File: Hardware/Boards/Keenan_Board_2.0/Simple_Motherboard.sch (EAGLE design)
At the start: 102 parts, among them U1 WIZ811MJ, U1_MUX 74HC4052D,653, U2_MUX 74HC4052D,653, U3_MUX 74HC4052D,653, U4_MUX 74HC4052D,653, U5_MUX 74HC4052D,653, U7_MUX 74HC4052D,653

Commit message: Top Stellaris Connector Routed
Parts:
- removed JP2, JP3: (no value), SparkFun-Connectors:M04POLAR
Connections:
- removed net N$23: JP2.2, U$2.PD3
- removed net N$24: JP2.3, U$2.PF0
- removed net N$25: JP3.1, U$2.PF1
- removed net N$26: JP3.2, U$2.PF2
- removed net N$27: JP3.3, U$2.PF3
- removed net N$30: JP3.4, U$2.PF4
- removed net N$7: JP2.1, U$2.PD2
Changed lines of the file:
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@@
 <part name="P+26" library="supply1" deviceset="+5V" device=""/>
 <part name="P+27" library="supply1" deviceset="+5V" device=""/>
-<part name="JP2" library="SparkFun-Connectors" deviceset="M04" device="POLAR"/>
-<part name="JP3" library="SparkFun-Connectors" deviceset="M04" device="POLAR"/>
 </parts>
 <sheets>
@@
 <instance part="S1" gate="1" x="-33.02" y="-35.56"/>
 <instance part="U$2" gate="G$1" x="0" y="0"/>
-<instance part="JP2" gate="G$1" x="88.9" y="5.08" rot="R180"/>
-<instance part="JP3" gate="G$1" x="88.9" y="-17.78" rot="R180"/>
 </instances>
 <busses>
@@
 </segment>
 </net>
-<net name="N$7" class="0">
-<segment>
-<pinref part="U$2" gate="G$1" pin="PD2"/>
-<wire x1="15.24" y1="5.08" x2="71.12" y2="5.08" width="0.1524" layer="91"/>
-<wire x1="71.12" y1="5.08" x2="71.12" y2="7.62" width="0.1524" layer="91"/>
-<pinref part="JP2" gate="G$1" pin="1"/>
-<wire x1="71.12" y1="7.62" x2="83.82" y2="7.62" width="0.1524" layer="91"/>
-</segment>
-</net>
-<net name="N$23" class="0">
-<segment>
-<pinref part="U$2" gate="G$1" pin="PD3"/>
-<wire x1="15.24" y1="2.54" x2="73.66" y2="2.54" width="0.1524" layer="91"/>
-<wire x1="73.66" y1="2.54" x2="73.66" y2="5.08" width="0.1524" layer="91"/>
-<pinref part="JP2" gate="G$1" pin="2"/>
-<wire x1="73.66" y1="5.08" x2="83.82" y2="5.08" width="0.1524" layer="91"/>
-</segment>
-</net>
-<net name="N$24" class="0">
-<segment>
-<pinref part="U$2" gate="G$1" pin="PF0"/>
-<wire x1="15.24" y1="-12.7" x2="76.2" y2="-12.7" width="0.1524" layer="91"/>
-<wire x1="76.2" y1="-12.7" x2="76.2" y2="2.54" width="0.1524" layer="91"/>
-<pinref part="JP2" gate="G$1" pin="3"/>
-<wire x1="76.2" y1="2.54" x2="83.82" y2="2.54" width="0.1524" layer="91"/>
-</segment>
-</net>
-<net name="N$25" class="0">
-<segment>
-<pinref part="U$2" gate="G$1" pin="PF1"/>
-<pinref part="JP3" gate="G$1" pin="1"/>
-<wire x1="15.24" y1="-15.24" x2="83.82" y2="-15.24" width="0.1524" layer="91"/>
-</segment>
-</net>
-<net name="N$26" class="0">
-<segment>
-<pinref part="JP3" gate="G$1" pin="2"/>
-<pinref part="U$2" gate="G$1" pin="PF2"/>
-<wire x1="83.82" y1="-17.78" x2="15.24" y2="-17.78" width="0.1524" layer="91"/>
-</segment>
-</net>
-<net name="N$27" class="0">
-<segment>
-<pinref part="JP3" gate="G$1" pin="3"/>
-<pinref part="U$2" gate="G$1" pin="PF3"/>
-<wire x1="83.82" y1="-20.32" x2="15.24" y2="-20.32" width="0.1524" layer="91"/>
-</segment>
-</net>
-<net name="N$30" class="0">
-<segment>
-<pinref part="JP3" gate="G$1" pin="4"/>
-<pinref part="U$2" gate="G$1" pin="PF4"/>
-<wire x1="83.82" y1="-22.86" x2="15.24" y2="-22.86" width="0.1524" layer="91"/>
-</segment>
-</net>

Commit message: Lots of stuff
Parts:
- added C27, C28: 0.1uF, SparkFun-Passives:CAP1206
- added C29, C30: 22pF, SparkFun-Passives:CAP1206
- added GPS: M09, SparkFun-Connectors:M09
- added J1: AVR_SPI_PRG_6PTH, SparkFun-Connectors:AVR_SPI_PRG_6PTH
- added R38: 10k, SparkFun-Resistors:RESISTOR1206
- added U2: ATMEGA328P_PDIP, SparkFun-DigitalIC:ATMEGA328P_PDIP
- added Y1: 16MHz, SparkFun-FreqCtrl:CRYSTALHC49US
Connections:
- removed net N$10 (its old number): R4.1, RS-485-2.A, U$4.1
- removed net N$11 (its old number): R4.2, RS-485-2.B, U$4.2
- removed net N$13 (its old number): R7.2, RS-485-3.Z, U$5.6
- removed net N$16 (its old number): R7.1, RS-485-3.Y, U$5.3
- removed net N$18 (its old number): R8.1, RS-485-4.A, U$6.1
- removed net N$19 (its old number): R8.2, RS-485-4.B, U$6.2
- new net 328_RX: U2.PD0(RXD)
- new net 328_TX: U2.PD1(TXD)
- new net ATCLK3: C30.1, U2.PB7(XTAL2/TOSC2), Y1.1
- new net ATCLK4: C29.1, U2.PB6(XTAL1/TOSC1), Y1.2
- new net AT_MISO: J1.1, U2.PB4(MISO)
- new net AT_MOSI: J1.4, U2.PB3(MOSI/OC2)
- new net AT_SCK: J1.3, U2.PB5(SCK)
- new net N$12: R8.1, RS-485-3.Y, U$5.3
- new net N$22: R3.1, RS-485-2.A, U$4.1
- new net N$23: U$2.PF0
- new net N$24: U$2.PF1
- new net N$25: U$2.PF2
- new net N$26: U$2.PF3
- new net N$27: U$2.PF4
- new net N$28: R3.2, RS-485-2.B, U$4.2
- new net N$34: R7.1, RS-485-4.A, U$6.1
- new net N$35: R7.2, RS-485-4.B, U$6.2
- new net N$7: U$2.PD3
- new net N$8: R8.2, RS-485-3.Z, U$5.6
- net +5V: now also C27.1, C28.1, J1.2, R38.2, U2.AREF, U2.AVCC, U2.VCC
- net 10_RX+: now also R27.2, RS_TRANS_8.A; no longer R32.2, RS_TRANS_10.A
- net 10_RX-: now also R27.1, RS_TRANS_8.B; no longer R32.1, RS_TRANS_10.B
- net 10_TX+: now also R29.1, RS_TRANS_8.Y; no longer R33.1, RS_TRANS_10.Y
- net 10_TX-: now also R29.2, RS_TRANS_8.Z; no longer R33.2, RS_TRANS_10.Z
- net 11_RX+: now also R31.2, RS_TRANS_10.A; no longer R34.2, RS_TRANS_11.A
- net 11_RX-: now also R31.1, RS_TRANS_10.B; no longer R34.1, RS_TRANS_11.B
- net 11_TX+: now also R33.1, RS_TRANS_10.Y; no longer R35.1, RS_TRANS_11.Y
- net 11_TX-: now also R33.2, RS_TRANS_10.Z; no longer R35.2, RS_TRANS_11.Z
- net 12_RX+: now also R35.2; no longer R36.2
- net 12_RX-: now also R35.1; no longer R36.1
- net 1_TX+: now also R16.1; no longer R15.1
- net 1_TX-: now also R16.2; no longer R15.2
- net 2_RX+: now also R18.2, RS_TRANS_3.A; no longer R16.2, RS_TRANS_2.A
- net 2_RX-: now also R18.1, RS_TRANS_3.B; no longer R16.1, RS_TRANS_2.B
- net 2_TX+: now also R20.1, RS_TRANS_3.Y; no longer R17.1, RS_TRANS_2.Y
- net 2_TX-: now also R20.2, RS_TRANS_3.Z; no longer R17.2, RS_TRANS_2.Z
- net 3_RX+: now also R22.2, RS_TRANS_5.A; no longer R18.2, RS_TRANS_3.A
- net 3_RX-: now also R22.1, RS_TRANS_5.B; no longer R18.1, RS_TRANS_3.B
- net 3_TX+: now also R24.1, RS_TRANS_5.Y; no longer R19.1, RS_TRANS_3.Y
- net 3_TX-: now also R24.2, RS_TRANS_5.Z; no longer R19.2, RS_TRANS_3.Z
- net 4_RX+: now also R26.2, RS_TRANS_7.A; no longer R20.2, RS_TRANS_4.A
- net 4_RX-: now also R26.1, RS_TRANS_7.B; no longer R20.1, RS_TRANS_4.B
- net 4_TX+: now also R28.1, RS_TRANS_7.Y; no longer R21.1, RS_TRANS_4.Y
- net 4_TX-: now also R28.2, RS_TRANS_7.Z; no longer R21.2, RS_TRANS_4.Z
- net 5_RX+: now also R30.2, RS_TRANS_9.A; no longer R22.2, RS_TRANS_5.A
- net 5_RX-: now also R30.1, RS_TRANS_9.B; no longer R22.1, RS_TRANS_5.B
- net 5_TX+: now also R32.1, RS_TRANS_9.Y; no longer R23.1, RS_TRANS_5.Y
- net 5_TX-: now also R32.2, RS_TRANS_9.Z; no longer R23.2, RS_TRANS_5.Z
- net 6_RX+: now also R34.2, RS_TRANS_11.A; no longer R24.2, RS_TRANS_6.A
- net 6_RX-: now also R34.1, RS_TRANS_11.B; no longer R24.1, RS_TRANS_6.B
- net 6_TX+: now also R36.1, RS_TRANS_11.Y; no longer R25.1, RS_TRANS_6.Y
- net 6_TX-: now also R36.2, RS_TRANS_11.Z; no longer R25.2, RS_TRANS_6.Z
- net 7_RX+: now also R15.2, RS_TRANS_2.A; no longer R26.2, RS_TRANS_7.A
- net 7_RX-: now also R15.1, RS_TRANS_2.B; no longer R26.1, RS_TRANS_7.B
- net 7_TX+: now also R17.1, RS_TRANS_2.Y; no longer R27.1, RS_TRANS_7.Y
- net 7_TX-: now also R17.2, RS_TRANS_2.Z; no longer R27.2, RS_TRANS_7.Z
- net 8_RX+: now also R19.2, RS_TRANS_4.A; no longer R28.2, RS_TRANS_8.A
- net 8_RX-: now also R19.1, RS_TRANS_4.B; no longer R28.1, RS_TRANS_8.B
- net 8_TX+: now also R21.1, RS_TRANS_4.Y; no longer R29.1, RS_TRANS_8.Y
- net 8_TX-: now also R21.2, RS_TRANS_4.Z; no longer R29.2, RS_TRANS_8.Z
- net 9_RX+: now also R23.2, RS_TRANS_6.A; no longer R30.2, RS_TRANS_9.A
- net 9_RX-: now also R23.1, RS_TRANS_6.B; no longer R30.1, RS_TRANS_9.B
- net 9_TX+: now also R25.1, RS_TRANS_6.Y; no longer R31.1, RS_TRANS_9.Y
- net 9_TX-: now also R25.2, RS_TRANS_6.Z; no longer R31.2, RS_TRANS_9.Z
- net GND: now also C27.2, C28.2, C29.2, C30.2, J1.6, U2.GND@1, U2.GND@2
- net N$4: now also R4.1; no longer R3.1
- net N$9: now also R4.2; no longer R3.2
- net RESET: now also J1.5, R38.1, U2.PC6(/RESET)
- net RS485_10_RX: now also RS_TRANS_8.R0; no longer RS_TRANS_10.R0
- net RS485_10_TX: now also RS_TRANS_8.DI; no longer RS_TRANS_10.DI
- net RS485_11_RX: now also RS_TRANS_10.R0; no longer RS_TRANS_11.R0
- net RS485_11_TX: now also RS_TRANS_10.DI; no longer RS_TRANS_11.DI
- net RS485_14_RX: now also RS-485-3.R0; no longer RS-485-2.R0
- net RS485_14_TX: now also RS-485-3.DI; no longer RS-485-2.DI
- net RS485_15_RX: now also RS-485-5.R0; no longer RS-485-3.R0
- net RS485_15_TX: now also RS-485-5.DI; no longer RS-485-3.DI
- net RS485_16_RX: now also RS-485-6.R0; no longer RS-485-4.R0
- net RS485_16_TX: now also RS-485-6.DI; no longer RS-485-4.DI
- net RS485_17_RX: now also RS-485-2.R0; no longer RS-485-5.R0
- net RS485_17_TX: now also RS-485-2.DI; no longer RS-485-5.DI
- net RS485_18_RX: now also RS-485-4.R0; no longer RS-485-6.R0
- net RS485_18_TX: now also RS-485-4.DI; no longer RS-485-6.DI
- net RS485_2_RX: now also RS_TRANS_3.R0; no longer RS_TRANS_2.R0
- net RS485_2_TX: now also RS_TRANS_3.DI; no longer RS_TRANS_2.DI
- net RS485_3_RX: now also RS_TRANS_5.R0; no longer RS_TRANS_3.R0
- net RS485_3_TX: now also RS_TRANS_5.DI; no longer RS_TRANS_3.DI
- net RS485_4_RX: now also RS_TRANS_7.R0; no longer RS_TRANS_4.R0
- net RS485_4_TX: now also RS_TRANS_7.DI; no longer RS_TRANS_4.DI
- net RS485_5_RX: now also RS_TRANS_9.R0; no longer RS_TRANS_5.R0
- net RS485_5_TX: now also RS_TRANS_9.DI; no longer RS_TRANS_5.DI
- net RS485_6_RX: now also RS_TRANS_11.R0; no longer RS_TRANS_6.R0
- net RS485_6_TX: now also RS_TRANS_11.DI; no longer RS_TRANS_6.DI
- net RS485_7_RX: now also RS_TRANS_2.R0; no longer RS_TRANS_7.R0
- net RS485_7_TX: now also RS_TRANS_2.DI; no longer RS_TRANS_7.DI
- net RS485_8_RX: now also RS_TRANS_4.R0; no longer RS_TRANS_8.R0
- net RS485_8_TX: now also RS_TRANS_4.DI; no longer RS_TRANS_8.DI
- net RS485_9_RX: now also RS_TRANS_6.R0; no longer RS_TRANS_9.R0
- net RS485_9_TX: now also RS_TRANS_6.DI; no longer RS_TRANS_9.DI

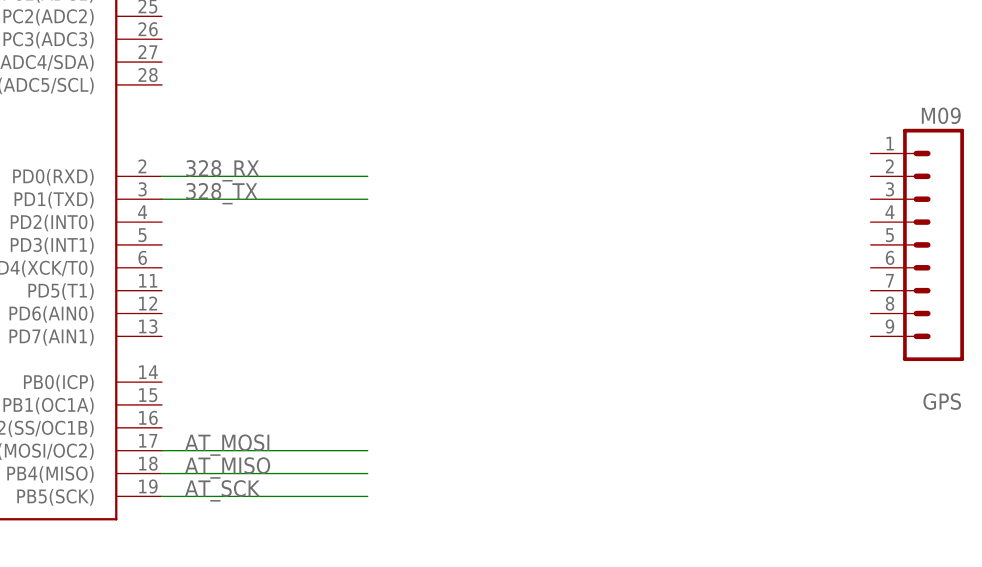
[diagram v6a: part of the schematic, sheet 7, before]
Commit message: Added GPS to schematic
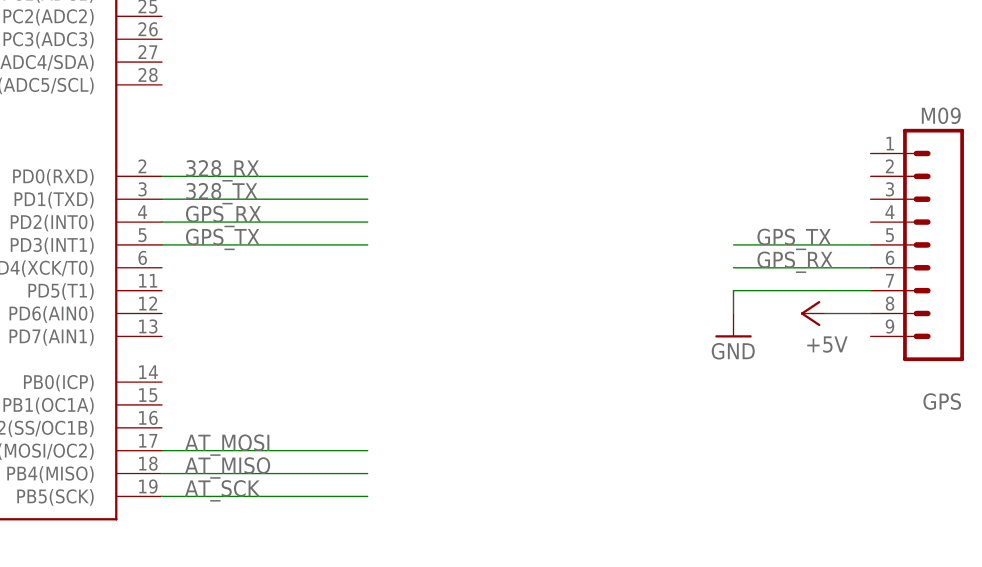
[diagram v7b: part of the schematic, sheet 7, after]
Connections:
- new net GPS_RX: GPS.6, U2.PD2(INT0)
- new net GPS_TX: GPS.5, U2.PD3(INT1)
- net +5V: now also GPS.8
- net GND: now also GPS.7
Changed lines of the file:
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@@
 <part name="GND35" library="supply1" deviceset="GND" device=""/>
 <part name="GPS" library="SparkFun-Connectors" deviceset="M09" device=""/>
+<part name="P+31" library="supply1" deviceset="+5V" device=""/>
+<part name="GND36" library="supply1" deviceset="GND" device=""/>
 </parts>
 <sheets>
@@
 <instance part="GND35" gate="1" x="25.4" y="-73.66"/>
 <instance part="GPS" gate="G$1" x="114.3" y="-5.08" rot="R180"/>
+<instance part="P+31" gate="1" x="96.52" y="-12.7" rot="R90"/>
+<instance part="GND36" gate="1" x="88.9" y="-15.24"/>
 </instances>
 <busses>
@@
 <wire x1="25.4" y1="-63.5" x2="25.4" y2="-71.12" width="0.1524" layer="91"/>
 </segment>
+<segment>
+<pinref part="GND36" gate="1" pin="GND"/>
+<wire x1="88.9" y1="-12.7" x2="88.9" y2="-10.16" width="0.1524" layer="91"/>
+<pinref part="GPS" gate="G$1" pin="7"/>
+<wire x1="88.9" y1="-10.16" x2="104.14" y2="-10.16" width="0.1524" layer="91"/>
+</segment>
 </net>
 <net name="ATCLK3" class="0">
@@
 <wire x1="25.4" y1="-58.42" x2="25.4" y2="-53.34" width="0.1524" layer="91"/>
 </segment>
+<segment>
+<pinref part="P+31" gate="1" pin="+5V"/>
+<pinref part="GPS" gate="G$1" pin="8"/>
+<wire x1="99.06" y1="-12.7" x2="104.14" y2="-12.7" width="0.1524" layer="91"/>
+</segment>
 </net>
 <net name="328_RX" class="0">
@@
 </segment>
 </net>
+<net name="GPS_RX" class="0">
+<segment>
+<pinref part="GPS" gate="G$1" pin="6"/>
+<wire x1="104.14" y1="-7.62" x2="88.9" y2="-7.62" width="0.1524" layer="91"/>
+<label x="91.44" y="-7.62" size="1.778" layer="95"/>
+</segment>
+<segment>
+<pinref part="U2" gate="G$1" pin="PD2(INT0)"/>
+<wire x1="25.4" y1="-2.54" x2="48.26" y2="-2.54" width="0.1524" layer="91"/>
+<label x="27.94" y="-2.54" size="1.778" layer="95"/>
+</segment>
+</net>
+<net name="GPS_TX" class="0">
+<segment>
+<pinref part="GPS" gate="G$1" pin="5"/>
+<wire x1="104.14" y1="-5.08" x2="88.9" y2="-5.08" width="0.1524" layer="91"/>
+<label x="91.44" y="-5.08" size="1.778" layer="95"/>
+</segment>
+<segment>
+<pinref part="U2" gate="G$1" pin="PD3(INT1)"/>
+<wire x1="25.4" y1="-5.08" x2="48.26" y2="-5.08" width="0.1524" layer="91"/>
+<label x="27.94" y="-5.08" size="1.778" layer="95"/>
+</segment>
+</net>
